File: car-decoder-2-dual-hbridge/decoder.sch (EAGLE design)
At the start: 46 parts, among them U1 MPC17531-ES, U2 RFM69CW, U3 MCP73831, U4 ATMEGA328P, U5 MPC17531-ES, U6 MIC5219 3.3V, Y1 16MHZ

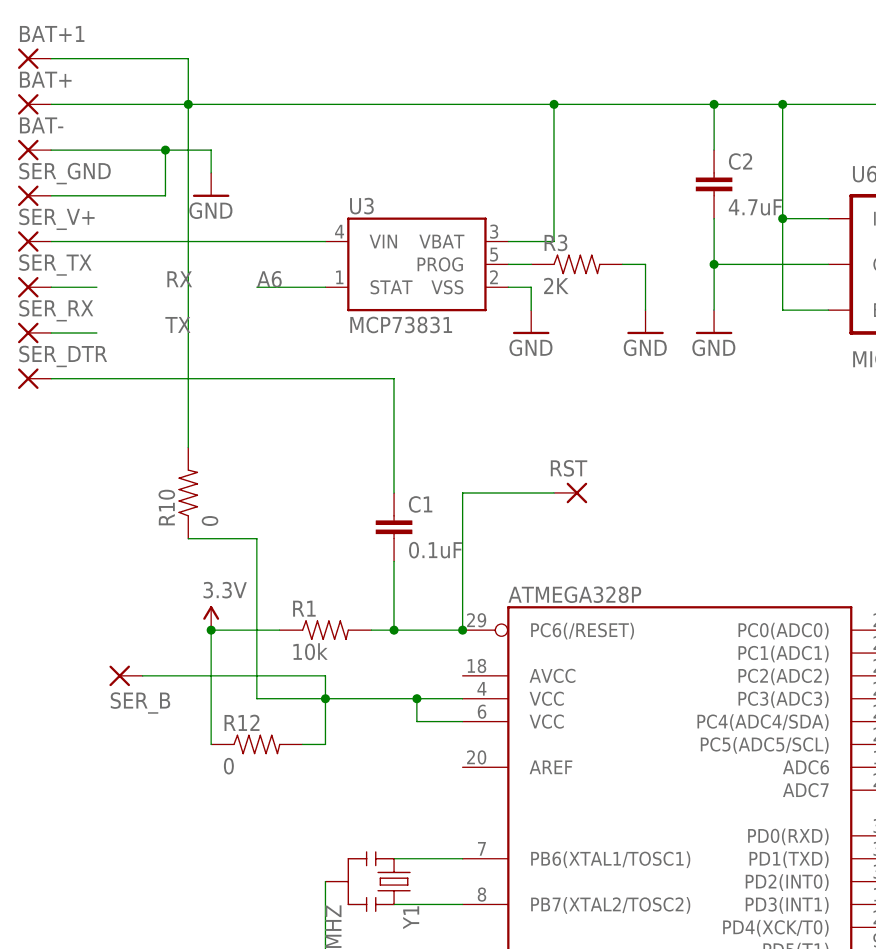
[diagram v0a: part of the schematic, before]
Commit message: New layout for RFM69HC
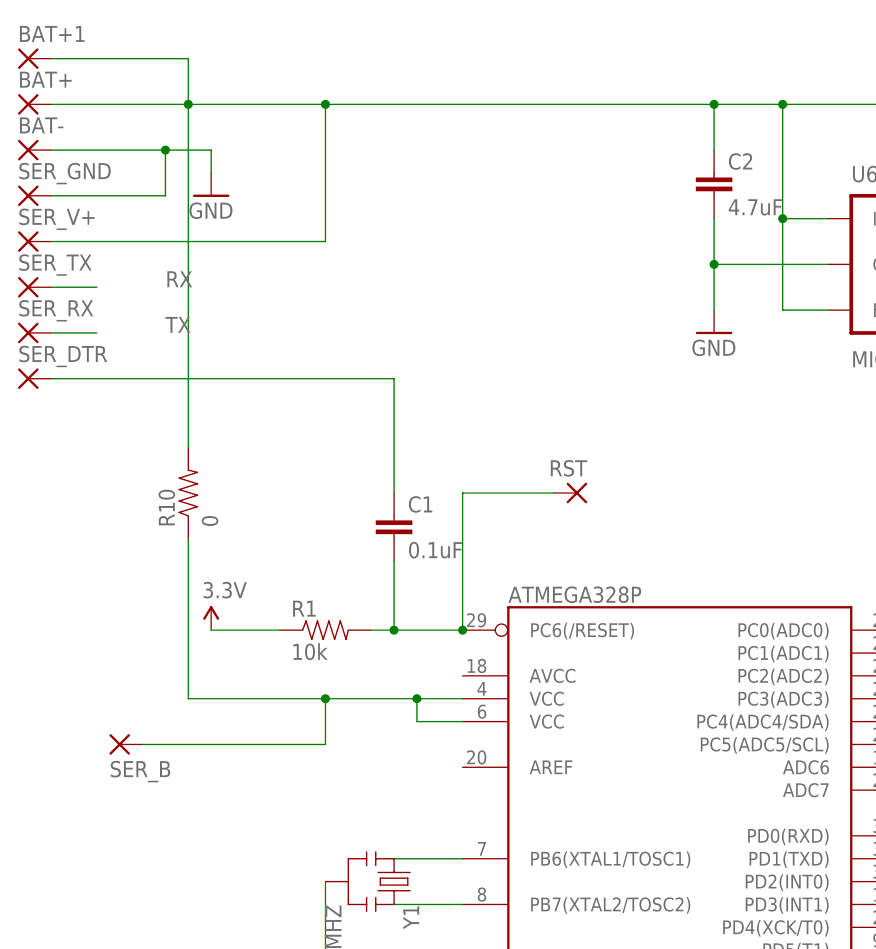
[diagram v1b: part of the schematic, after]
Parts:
- removed R12: 0, SparkFun-Resistors:RESISTOR0603-RES
- removed R3: 2K, SparkFun-Resistors:RESISTOR0603-RES
- removed U3: MCP73831, SparkFun-PowerIC:MCP73831
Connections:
- removed net N$11: R3.1, U3.PROG
- removed net N$9: SER_V+.P, U3.VIN
- net A6: no longer U3.STAT
- net BAT+: now also SER_V+.P; no longer U3.VBAT
- net GND: no longer R3.2, U3.VSS
- net N$8: no longer R12.2
- net VCC: no longer R12.1
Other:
- moved on the sheet: SER_B
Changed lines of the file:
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@@
 <part name="BAT+" library="wirepad" deviceset="SMD2" device=""/>
 <part name="GND4" library="SparkFun-Aesthetics" deviceset="GND" device=""/>
-<part name="U3" library="SparkFun-PowerIC" deviceset="MCP73831" device=""/>
-<part name="GND5" library="SparkFun-Aesthetics" deviceset="GND" device=""/>
-<part name="GND6" library="SparkFun-Aesthetics" deviceset="GND" device=""/>
-<part name="R3" library="SparkFun-Resistors" deviceset="RESISTOR" device="0603-RES" value="2K"/>
 <part name="U6" library="SparkFun-PowerIC" deviceset="V_REG_MIC5219" device="3.3V" value="MIC5219 3.3V"/>
 <part name="GND7" library="SparkFun-Aesthetics" deviceset="GND" device=""/>
@@
 <part name="RST" library="wirepad" deviceset="SMD2" device=""/>
 <part name="R10" library="SparkFun-Resistors" deviceset="RESISTOR" device="0603-RES" value="0"/>
-<part name="R12" library="SparkFun-Resistors" deviceset="RESISTOR" device="0603-RES" value="0"/>
 <part name="R13" library="SparkFun-Resistors" deviceset="RESISTOR" device="0603-RES" value="10k"/>
 <part name="BAT+1" library="wirepad" deviceset="SMD2" device=""/>
@@
 <instance part="BAT+" gate="1" x="-17.78" y="132.08"/>
 <instance part="GND4" gate="1" x="2.54" y="121.92"/>
-<instance part="U3" gate="G$1" x="25.4" y="114.3"/>
-<instance part="GND5" gate="1" x="38.1" y="106.68"/>
-<instance part="GND6" gate="1" x="50.8" y="106.68"/>
-<instance part="R3" gate="G$1" x="43.18" y="114.3"/>
 <instance part="U6" gate="G$1" x="81.28" y="114.3"/>
 <instance part="GND7" gate="1" x="58.42" y="106.68"/>
@@
 <instance part="RST" gate="1" x="43.18" y="88.9" rot="MR0"/>
 <instance part="R10" gate="G$1" x="0" y="88.9" rot="R90"/>
-<instance part="R12" gate="G$1" x="7.62" y="60.96"/>
 <instance part="R13" gate="G$1" x="15.24" y="-20.32"/>
 <instance part="BAT+1" gate="1" x="-17.78" y="137.16"/>
-<instance part="SER_B" gate="1" x="-7.62" y="68.58" rot="MR180"/>
+<instance part="SER_B" gate="1" x="-7.62" y="60.96" rot="MR180"/>
 <instance part="U1" gate="G$1" x="137.16" y="-22.86"/>
 <instance part="U5" gate="G$1" x="137.16" y="33.02"/>
@@
 <wire x1="10.16" y1="73.66" x2="2.54" y2="73.66" width="0.1524" layer="91"/>
 <pinref part="VCC4" gate="G$1" pin="VCC"/>
-<pinref part="R12" gate="G$1" pin="1"/>
-<wire x1="2.54" y1="60.96" x2="2.54" y2="73.66" width="0.1524" layer="91"/>
-<junction x="2.54" y="73.66"/>
 </segment>
 <segment>
@@
 <wire x1="-2.54" y1="121.92" x2="-2.54" y2="127" width="0.1524" layer="91"/>
 <junction x="-2.54" y="127"/>
-</segment>
-<segment>
-<pinref part="U3" gate="G$1" pin="VSS"/>
-<wire x1="35.56" y1="111.76" x2="38.1" y2="111.76" width="0.1524" layer="91"/>
-<pinref part="GND5" gate="1" pin="GND"/>
-<wire x1="38.1" y1="111.76" x2="38.1" y2="109.22" width="0.1524" layer="91"/>
-</segment>
-<segment>
-<pinref part="R3" gate="G$1" pin="2"/>
-<wire x1="48.26" y1="114.3" x2="50.8" y2="114.3" width="0.1524" layer="91"/>
-<pinref part="GND6" gate="1" pin="GND"/>
-<wire x1="50.8" y1="114.3" x2="50.8" y2="109.22" width="0.1524" layer="91"/>
 </segment>
 <segment>
@@
 </segment>
 </net>
-<net name="N$9" class="0">
-<segment>
-<pinref part="U3" gate="G$1" pin="VIN"/>
-<pinref part="SER_V+" gate="1" pin="P"/>
-<wire x1="15.24" y1="116.84" x2="-15.24" y2="116.84" width="0.1524" layer="91"/>
-</segment>
-</net>
-<net name="N$11" class="0">
-<segment>
-<pinref part="U3" gate="G$1" pin="PROG"/>
-<pinref part="R3" gate="G$1" pin="1"/>
-<wire x1="35.56" y1="114.3" x2="38.1" y2="114.3" width="0.1524" layer="91"/>
-</segment>
-</net>
 <net name="D5" class="0">
 <segment>
@@
 <wire x1="66.04" y1="119.38" x2="71.12" y2="119.38" width="0.1524" layer="91"/>
 <pinref part="BAT+" gate="1" pin="P"/>
-<junction x="40.64" y="132.08"/>
 <wire x1="-15.24" y1="132.08" x2="0" y2="132.08" width="0.1524" layer="91"/>
-<wire x1="0" y1="132.08" x2="40.64" y2="132.08" width="0.1524" layer="91"/>
-<wire x1="40.64" y1="132.08" x2="58.42" y2="132.08" width="0.1524" layer="91"/>
+<wire x1="0" y1="132.08" x2="15.24" y2="132.08" width="0.1524" layer="91"/>
+<wire x1="15.24" y1="132.08" x2="58.42" y2="132.08" width="0.1524" layer="91"/>
 <wire x1="58.42" y1="132.08" x2="66.04" y2="132.08" width="0.1524" layer="91"/>
 <wire x1="66.04" y1="132.08" x2="129.54" y2="132.08" width="0.1524" layer="91"/>
-<wire x1="40.64" y1="132.08" x2="40.64" y2="116.84" width="0.1524" layer="91"/>
-<pinref part="U3" gate="G$1" pin="VBAT"/>
-<wire x1="40.64" y1="116.84" x2="35.56" y2="116.84" width="0.1524" layer="91"/>
 <wire x1="66.04" y1="119.38" x2="66.04" y2="132.08" width="0.1524" layer="91"/>
 <junction x="66.04" y="119.38"/>
@@
 <wire x1="149.86" y1="-35.56" x2="154.94" y2="-35.56" width="0.1524" layer="91"/>
 <junction x="154.94" y="-35.56"/>
+<pinref part="SER_V+" gate="1" pin="P"/>
+<wire x1="15.24" y1="116.84" x2="-15.24" y2="116.84" width="0.1524" layer="91"/>
+<wire x1="15.24" y1="116.84" x2="15.24" y2="132.08" width="0.1524" layer="91"/>
+<junction x="15.24" y="132.08"/>
 </segment>
 </net>
@@
 <label x="83.82" y="58.42" size="1.778" layer="95"/>
 </segment>
-<segment>
-<pinref part="U3" gate="G$1" pin="STAT"/>
-<wire x1="15.24" y1="111.76" x2="7.62" y2="111.76" width="0.1524" layer="91"/>
-<label x="7.62" y="111.76" size="1.778" layer="95"/>
-</segment>
 </net>
 <net name="A7" class="0">
@@
 <junction x="25.4" y="66.04"/>
 <wire x1="25.4" y1="66.04" x2="15.24" y2="66.04" width="0.1524" layer="91"/>
-<wire x1="15.24" y1="66.04" x2="7.62" y2="66.04" width="0.1524" layer="91"/>
+<wire x1="15.24" y1="66.04" x2="0" y2="66.04" width="0.1524" layer="91"/>
 <junction x="15.24" y="66.04"/>
-<wire x1="15.24" y1="60.96" x2="15.24" y2="66.04" width="0.1524" layer="91"/>
-<pinref part="R12" gate="G$1" pin="2"/>
-<wire x1="12.7" y1="60.96" x2="15.24" y2="60.96" width="0.1524" layer="91"/>
-<wire x1="7.62" y1="66.04" x2="7.62" y2="83.82" width="0.1524" layer="91"/>
+<wire x1="0" y1="66.04" x2="0" y2="83.82" width="0.1524" layer="91"/>
 <pinref part="R10" gate="G$1" pin="1"/>
-<wire x1="7.62" y1="83.82" x2="0" y2="83.82" width="0.1524" layer="91"/>
-<wire x1="15.24" y1="66.04" x2="15.24" y2="68.58" width="0.1524" layer="91"/>
+<wire x1="15.24" y1="66.04" x2="15.24" y2="60.96" width="0.1524" layer="91"/>
 <pinref part="SER_B" gate="1" pin="P"/>
-<wire x1="15.24" y1="68.58" x2="-5.08" y2="68.58" width="0.1524" layer="91"/>
-</segment>
-</net>
+<wire x1="15.24" y1="60.96" x2="-5.08" y2="60.96" width="0.1524" layer="91"/>
+</segment>
+</net>
